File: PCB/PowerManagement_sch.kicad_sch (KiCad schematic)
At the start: 10 parts, among them U2 SGM2050XTRL20G/TR

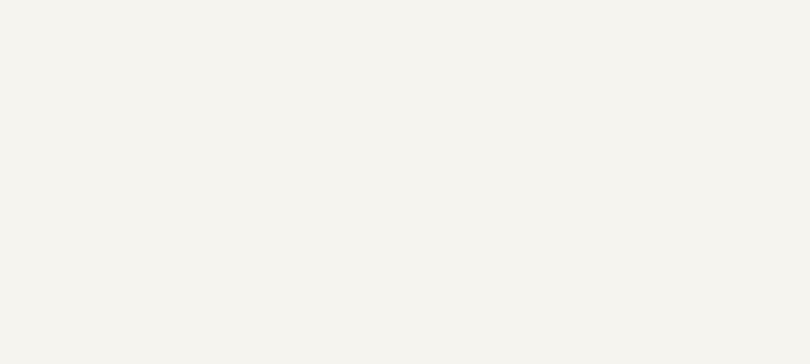
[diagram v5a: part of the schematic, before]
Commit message: silkscreen done
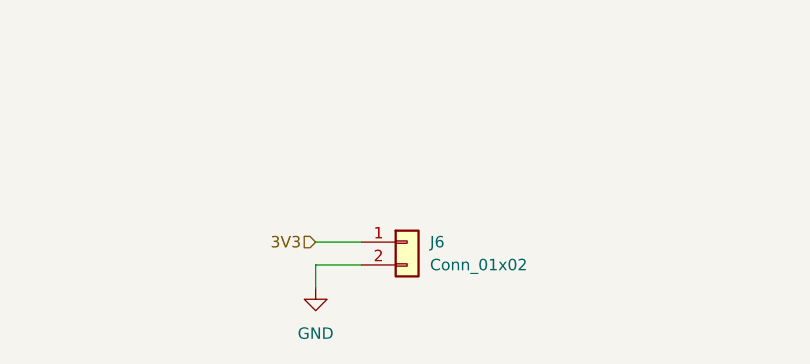
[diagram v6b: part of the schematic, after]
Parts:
- added J6: Conn_01x02, Connector_PinHeader_2.54mm:PinHeader_1x02_P2.54mm_Vertical, symbol Connector_Generic:Conn_01x02
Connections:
- net 3V3: now also J6.1 (Pin_1)
- net GND: now also J6.2 (Pin_2)
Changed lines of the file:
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@@
+	(wire
+		(pts
+			(xy 80.01 119.38) (xy 85.09 119.38)
+		)
+		(stroke
+			(width 0)
+			(type default)
+		)
+	)
 	(wire
 		(pts
@@
 	(wire
 		(pts
+			(xy 80.01 121.92) (xy 85.09 121.92)
+		)
+		(stroke
+			(width 0)
+			(type default)
+		)
+	)
+	(wire
+		(pts
 			(xy 35.56 68.58) (xy 82.55 68.58)
+		)
+		(stroke
+			(width 0)
+			(type default)
+		)
+	)
+	(wire
+		(pts
+			(xy 80.01 124.46) (xy 80.01 121.92)
 		)
 		(stroke
@@
 			)
 			(justify left)
+		)
+	)
+	(hierarchical_label "3V3"
+		(shape input)
+		(at 80.01 119.38 180)
+		(effects
+			(font
+				(size 1.27 1.27)
+			)
+			(justify right)
 		)
 	)
@@
 				(path "/64c66767-4367-4391-b4db-5d3ae338f23b/2ffef3f0-c596-4316-9d55-314e15f9f8d2"
 					(reference "USB1")
+					(unit 1)
+				)
+			)
+		)
+	)
+	(symbol
+		(lib_id "power:GND")
+		(at 80.01 124.46 0)
+		(unit 1)
+		(exclude_from_sim no)
+		(in_bom yes)
+		(on_board yes)
+		(dnp no)
+		(fields_autoplaced yes)
+		(property "Reference" "#PWR02"
+			(at 80.01 130.81 0)
+			(effects
+				(font
+					(size 1.27 1.27)
+				)
+				(hide yes)
+			)
+		)
+		(property "Value" "GND"
+			(at 80.01 129.54 0)
+			(effects
+				(font
+					(size 1.27 1.27)
+				)
+			)
+		)
+		(property "Footprint" ""
+			(at 80.01 124.46 0)
+			(effects
+				(font
+					(size 1.27 1.27)
+				)
+				(hide yes)
+			)
+		)
+		(property "Datasheet" ""
+			(at 80.01 124.46 0)
+			(effects
+				(font
+					(size 1.27 1.27)
+				)
+				(hide yes)
+			)
+		)
+		(property "Description" "Power symbol creates a global label with name \"GND\" , ground"
+			(at 80.01 124.46 0)
+			(effects
+				(font
+					(size 1.27 1.27)
+				)
+				(hide yes)
+			)
+		)
+		(pin "1"
+		)
+		(instances
+			(project ""
+				(path "/64c66767-4367-4391-b4db-5d3ae338f23b/2ffef3f0-c596-4316-9d55-314e15f9f8d2"
+					(reference "#PWR02")
 					(unit 1)
 				)
@@
 					(unit 1)
 				)
+			)
+		)
+	)
+	(symbol
+		(lib_id "Connector_Generic:Conn_01x02")
+		(at 90.17 119.38 0)
+		(unit 1)
+		(exclude_from_sim no)
+		(in_bom yes)
+		(on_board yes)
+		(dnp no)
+		(fields_autoplaced yes)
+		(property "Reference" "J6"
+			(at 92.71 119.3799 0)
+			(effects
+				(font
+					(size 1.27 1.27)
+				)
+				(justify left)
+			)
+		)
+		(property "Value" "Conn_01x02"
+			(at 92.71 121.9199 0)
+			(effects
+				(font
+					(size 1.27 1.27)
+				)
+				(justify left)
+			)
+		)
+		(property "Footprint" "Connector_PinHeader_2.54mm:PinHeader_1x02_P2.54mm_Vertical"
+			(at 90.17 119.38 0)
+			(effects
+				(font
+					(size 1.27 1.27)
+				)
+				(hide yes)
+			)
+		)
+		(property "Datasheet" "~"
+			(at 90.17 119.38 0)
+			(effects
+				(font
+					(size 1.27 1.27)
+				)
+				(hide yes)
+			)
+		)
+		(property "Description" "Generic connector, single row, 01x02, script generated (kicad-library-utils/schlib/autogen/connector/)"
+			(at 90.17 119.38 0)
+			(effects
+				(font
+					(size 1.27 1.27)
+				)
+				(hide yes)
+			)
+		)
+		(pin "2"
+		)
+		(pin "1"
+		)
+		(instances
+			(project ""
+				(path "/64c66767-4367-4391-b4db-5d3ae338f23b/2ffef3f0-c596-4316-9d55-314e15f9f8d2"
+					(reference "J6")
+					(unit 1)
+				)

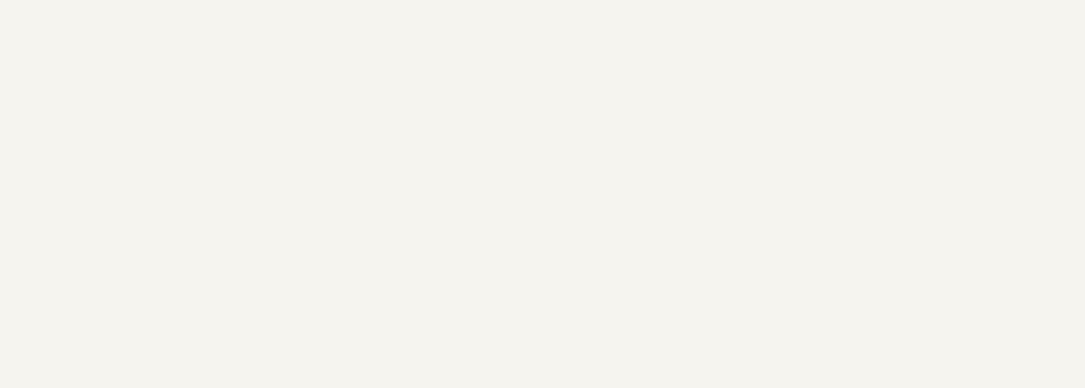
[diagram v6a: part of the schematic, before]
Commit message: added bulk caps + drc check
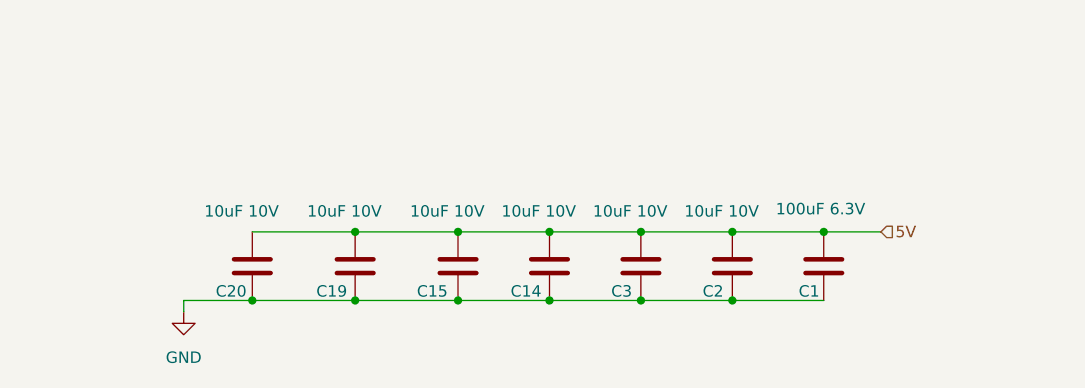
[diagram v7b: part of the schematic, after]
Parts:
- added C1: 100uF 6.3V, Capacitor_SMD:C_1206_3216Metric_Pad1.33x1.80mm_HandSolder, symbol Device:C
- added C14, C15, C19, C2, C20, C3: 10uF 10V, Capacitor_SMD:C_0402_1005Metric, symbol Device:C
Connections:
- net 5V: now also C1.1, C14.1, C15.1, C19.1, C2.1, C20.1, C3.1
- net GND: now also C1.2, C14.2, C15.2, C19.2, C2.2, C20.2, C3.2

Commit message: final checks for PCB, nearly ready to order v1
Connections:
- net 3V3: no longer D5.5
- net 5V: now also D5.5
- net GND: now also USB1.13 (SHELL), USB1.14 (SHELL)
- no-connect marks 10 -> 8
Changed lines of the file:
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@@
-	)
-	(no_connect
-		(at 25.4 33.02)
-	)
-	(no_connect
-		(at 25.4 60.96)
 	)
 	(no_connect
@@
 	(wire
 		(pts
+			(xy 24.13 33.02) (xy 25.4 33.02)
+		)
+		(stroke
+			(width 0)
+			(type default)
+		)
+	)
+	(wire
+		(pts
 			(xy 46.99 38.1) (xy 49.53 38.1)
 		)
@@
 	(wire
 		(pts
+			(xy 24.13 60.96) (xy 25.4 60.96)
+		)
+		(stroke
+			(width 0)
+			(type default)
+		)
+	)
+	(wire
+		(pts
 			(xy 52.07 43.18) (xy 54.61 43.18)
 		)
@@
 	(wire
 		(pts
-			(xy 127 67.31) (xy 132.08 67.31)
+			(xy 127 67.31) (xy 133.35 67.31)
 		)
 		(stroke
@@
 		)
 	)
-	(hierarchical_label "3V3"
+	(hierarchical_label "5V"
 		(shape input)
-		(at 132.08 67.31 0)
+		(at 133.35 67.31 0)
 		(effects
 			(font
@@
 				(path "/64c66767-4367-4391-b4db-5d3ae338f23b/2ffef3f0-c596-4316-9d55-314e15f9f8d2"
 					(reference "C20")
+					(unit 1)
+				)
+			)
+		)
+	)
+	(symbol
+		(lib_id "power:GND")
+		(at 24.13 33.02 0)
+		(unit 1)
+		(exclude_from_sim no)
+		(in_bom yes)
+		(on_board yes)
+		(dnp no)
+		(property "Reference" "#PWR05"
+			(at 24.13 39.37 0)
+			(effects
+				(font
+					(size 1.27 1.27)
+				)
+				(hide yes)
+			)
+		)
+		(property "Value" "GND"
+			(at 23.876 36.83 0)
+			(effects
+				(font
+					(size 1.27 1.27)
+				)
+			)
+		)
+		(property "Footprint" ""
+			(at 24.13 33.02 0)
+			(effects
+				(font
+					(size 1.27 1.27)
+				)
+				(hide yes)
+			)
+		)
+		(property "Datasheet" ""
+			(at 24.13 33.02 0)
+			(effects
+				(font
+					(size 1.27 1.27)
+				)
+				(hide yes)
+			)
+		)
+		(property "Description" "Power symbol creates a global label with name \"GND\" , ground"
+			(at 24.13 33.02 0)
+			(effects
+				(font
+					(size 1.27 1.27)
+				)
+				(hide yes)
+			)
+		)
+		(pin "1"
+		)
+		(instances
+			(project "detentOne"
+				(path "/64c66767-4367-4391-b4db-5d3ae338f23b/2ffef3f0-c596-4316-9d55-314e15f9f8d2"
+					(reference "#PWR05")
 					(unit 1)
 				)
@@
 					(unit 1)
 				)
+			)
+		)
+	)
+	(symbol
+		(lib_id "power:GND")
+		(at 24.13 60.96 0)
+		(unit 1)
+		(exclude_from_sim no)
+		(in_bom yes)
+		(on_board yes)
+		(dnp no)
+		(property "Reference" "#PWR06"
+			(at 24.13 67.31 0)
+			(effects
+				(font
+					(size 1.27 1.27)
+				)
+				(hide yes)
+			)
+		)
+		(property "Value" "GND"
+			(at 23.876 64.77 0)
+			(effects
+				(font
+					(size 1.27 1.27)
+				)
+			)
+		)
+		(property "Footprint" ""
+			(at 24.13 60.96 0)
+			(effects
+				(font
+					(size 1.27 1.27)
+				)
+				(hide yes)
+			)
+		)
+		(property "Datasheet" ""
+			(at 24.13 60.96 0)
+			(effects
+				(font
+					(size 1.27 1.27)
+				)
+				(hide yes)
+			)
+		)
+		(property "Description" "Power symbol creates a global label with name \"GND\" , ground"
+			(at 24.13 60.96 0)
+			(effects
+				(font
+					(size 1.27 1.27)
+				)
+				(hide yes)
+			)
+		)
+		(pin "1"
+		)
+		(instances
+			(project "detentOne"
+				(path "/64c66767-4367-4391-b4db-5d3ae338f23b/2ffef3f0-c596-4316-9d55-314e15f9f8d2"
+					(reference "#PWR06")
+					(unit 1)
+				)
